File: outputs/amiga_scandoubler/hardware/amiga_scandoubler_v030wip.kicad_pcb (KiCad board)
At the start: 4 copper layers, 95 x 95 mm, 135 parts, among them J1 33DSMT1-E15SNCT, J2 33DSMT1-E15SNCT, J3 TYPE-C-31-M-12, J4 JTAG 2x05 2.54mm, U1 TVP7002PZP, U2 GW1N-LV4QN88C6/I5, U3 ADV7125KSTZ140, U4 SN74LVC2G17DBVR, U5 SN74LVC2G17DBVR, U6 SN74LVC1G17DBVR, U7 TPS62160DSGR, U8 TPS62160DSGR, U9 TPS62160DSGR, Y1 27MHz ECS-3225MVLC

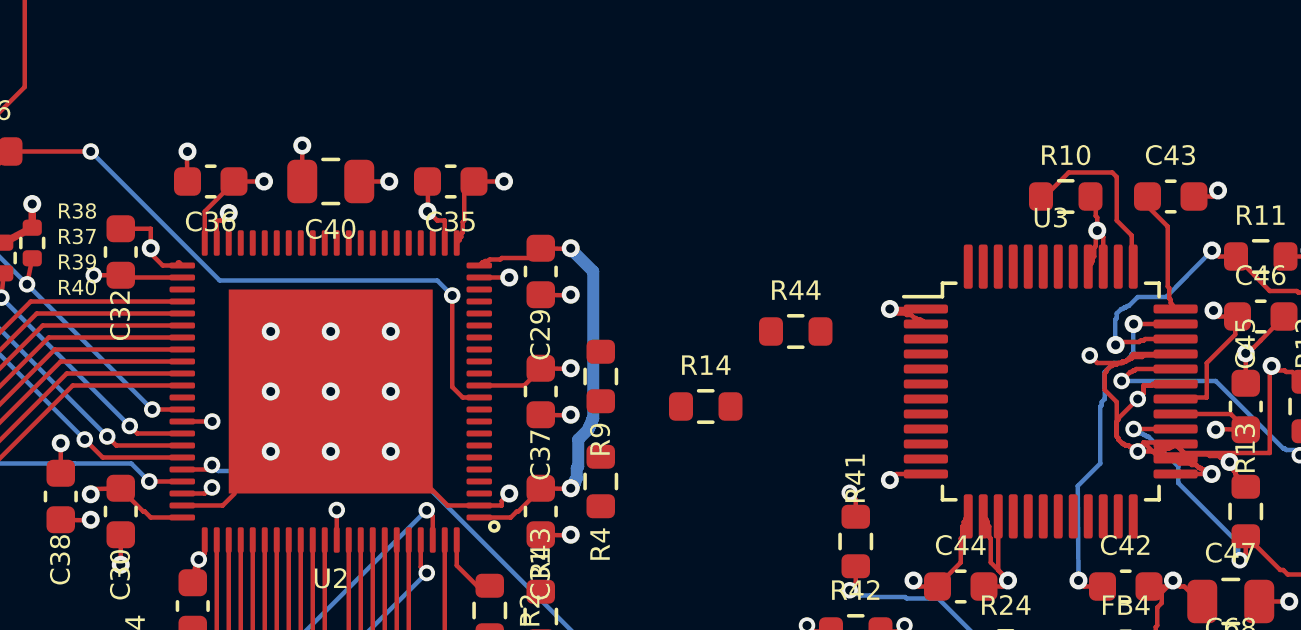
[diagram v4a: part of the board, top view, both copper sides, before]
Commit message: v030wip: 課題4 DAC_PSAVE_N(U2.56)を R44・U3.38 へ接続
- U2.56 → 内周ビア → B.Cu で EP 下 y=41 → 1V2 壁の北端を回って R44.1
- R44 → B.Cu y=39.85 → U3 本体下のビア → U3.38(パッド内側から)
- KiCad 7 DRC: エラー 0、未接続 97→95(DAC_PSAVE_N のみ)
- 導通確認、電源監査 PASS。DAC バス(課題6)への影響を記録

Co-Authored-By: Claude Opus 5.5 <noreply@anthropic.com>
Claude-Session: https://claude.ai/code/session_019f929sAJ7LRnJRRFvA6g9F
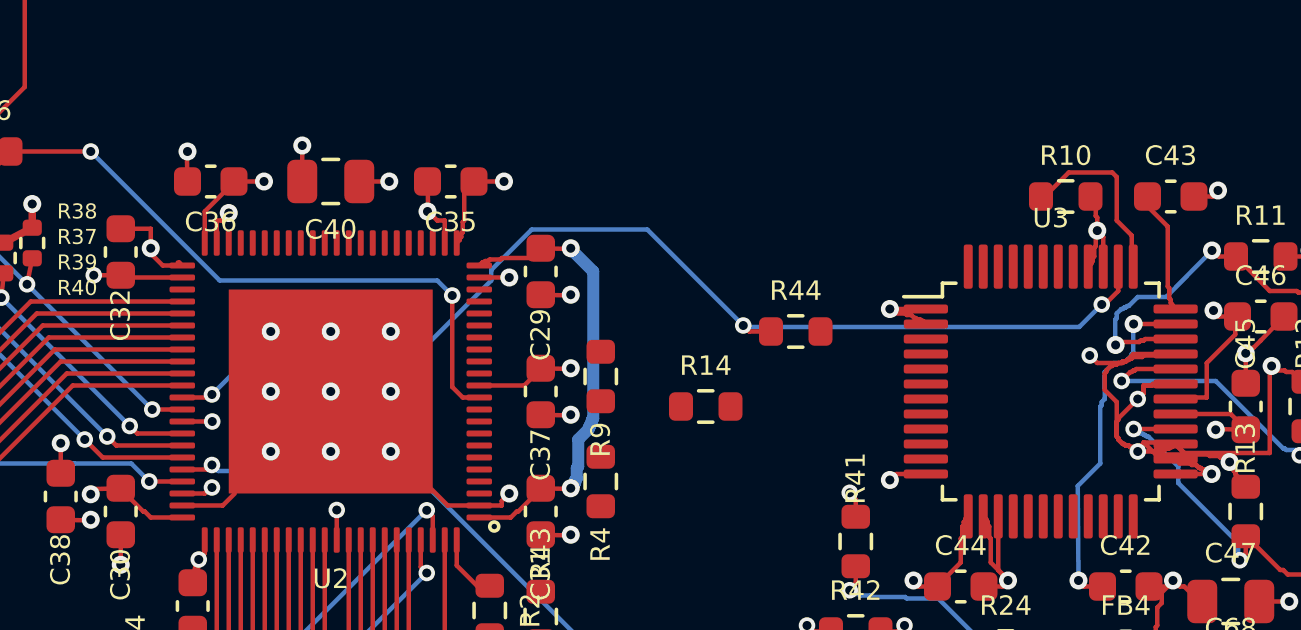
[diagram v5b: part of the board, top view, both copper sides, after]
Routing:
- net DAC_PSAVE_N: track 0.00 -> 37.4 mm, vias 0 -> 3
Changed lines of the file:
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@@
   (segment (start 54.2 47.8) (end 54.875 48.475) (width 0.15) (layer "F.Cu") (net 59))
   (segment (start 54.875 48.475) (end 55.3 48.475) (width 0.15) (layer "F.Cu") (net 59))
+  (segment (start 63.75 39.8) (end 63.95 40) (width 0.15) (layer "F.Cu") (net 60))
+  (segment (start 76.25 38.65) (end 76.25 37.837) (width 0.15) (layer "F.Cu") (net 60))
+  (segment (start 75.7 39.1) (end 75.8 39.1) (width 0.15) (layer "F.Cu") (net 60))
+  (segment (start 63.95 40) (end 64.675 40) (width 0.15) (layer "F.Cu") (net 60))
+  (segment (start 75.8 39.1) (end 76.25 38.65) (width 0.15) (layer "F.Cu") (net 60))
+  (segment (start 45.94 42.2) (end 46.04 42.1) (width 0.15) (layer "F.Cu") (net 60))
+  (segment (start 45.05 42.2) (end 45.94 42.2) (width 0.15) (layer "F.Cu") (net 60))
+  (via (at 75.7 39.1) (size 0.55) (drill 0.3) (layers "F.Cu" "B.Cu") (net 60))
+  (via (at 46.04 42.1) (size 0.55) (drill 0.3) (layers "F.Cu" "B.Cu") (net 60))
+  (via (at 63.75 39.8) (size 0.55) (drill 0.3) (layers "F.Cu" "B.Cu") (net 60))
+  (segment (start 46.04 42.1) (end 47.14 41) (width 0.15) (layer "B.Cu") (net 60))
+  (segment (start 63.8 39.85) (end 74.95 39.85) (width 0.15) (layer "B.Cu") (net 60))
+  (segment (start 56.7 36.6) (end 60.55 36.6) (width 0.15) (layer "B.Cu") (net 60))
+  (segment (start 60.55 36.6) (end 63.75 39.8) (width 0.15) (layer "B.Cu") (net 60))
+  (segment (start 63.75 39.8) (end 63.8 39.85) (width 0.15) (layer "B.Cu") (net 60))
+  (segment (start 55.35 38.3) (end 55.35 37.95) (width 0.15) (layer "B.Cu") (net 60))
+  (segment (start 55.35 37.95) (end 56.7 36.6) (width 0.15) (layer "B.Cu") (net 60))
+  (segment (start 52.65 41) (end 55.35 38.3) (width 0.15) (layer "B.Cu") (net 60))
+  (segment (start 47.14 41) (end 52.65 41) (width 0.15) (layer "B.Cu") (net 60))
+  (segment (start 74.95 39.85) (end 75.7 39.1) (width 0.15) (layer "B.Cu") (net 60))
   (segment (start 80.85 53.45) (end 80.65 53.25) (width 0.15) (layer "F.Cu") (net 62))
   (segment (start 67.5 48.4) (end 67.3 48.6) (width 0.15) (layer "F.Cu") (net 62))

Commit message: v030wip: 課題5の準備 — 1V2 右リンクを In2 へ、PSAVE を南回りへ変更
- 1V2 の右側 B.Cu 壁(58,37.225)↔(58,45.225)を同形状で In2.Cu へ移動
- DAC_PSAVE_N の U2→R44 区間を y=42.75 → 南東 → y=46 → 北東の経路に変更
  (JTAG を B.Cu で北上させる通路 x 55.4–60 を確保するため)
- KiCad 7 DRC: エラー 0、未接続 95 で変化なし。導通確認、電源監査 PASS
- 右辺の現状分析を CLAUDE.md に記録

Co-Authored-By: Claude Opus 5.5 <noreply@anthropic.com>
Claude-Session: https://claude.ai/code/session_019f929sAJ7LRnJRRFvA6g9F
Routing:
- net DAC_PSAVE_N: track 37.4 -> 38.9 mm
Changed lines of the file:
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@@
   (via (at 46.04 42.1) (size 0.55) (drill 0.3) (layers "F.Cu" "B.Cu") (net 60))
   (via (at 63.75 39.8) (size 0.55) (drill 0.3) (layers "F.Cu" "B.Cu") (net 60))
-  (segment (start 46.04 42.1) (end 47.14 41) (width 0.15) (layer "B.Cu") (net 60))
   (segment (start 63.8 39.85) (end 74.95 39.85) (width 0.15) (layer "B.Cu") (net 60))
-  (segment (start 56.7 36.6) (end 60.55 36.6) (width 0.15) (layer "B.Cu") (net 60))
-  (segment (start 60.55 36.6) (end 63.75 39.8) (width 0.15) (layer "B.Cu") (net 60))
+  (segment (start 59.45 46) (end 63.75 41.7) (width 0.15) (layer "B.Cu") (net 60))
+  (segment (start 55.7 46) (end 59.45 46) (width 0.15) (layer "B.Cu") (net 60))
+  (segment (start 46.04 42.1) (end 46.69 42.75) (width 0.15) (layer "B.Cu") (net 60))
   (segment (start 63.75 39.8) (end 63.8 39.85) (width 0.15) (layer "B.Cu") (net 60))
-  (segment (start 55.35 38.3) (end 55.35 37.95) (width 0.15) (layer "B.Cu") (net 60))
-  (segment (start 55.35 37.95) (end 56.7 36.6) (width 0.15) (layer "B.Cu") (net 60))
-  (segment (start 52.65 41) (end 55.35 38.3) (width 0.15) (layer "B.Cu") (net 60))
-  (segment (start 47.14 41) (end 52.65 41) (width 0.15) (layer "B.Cu") (net 60))
+  (segment (start 46.69 42.75) (end 52.45 42.75) (width 0.15) (layer "B.Cu") (net 60))
+  (segment (start 52.45 42.75) (end 55.7 46) (width 0.15) (layer "B.Cu") (net 60))
+  (segment (start 63.75 41.7) (end 63.75 39.8) (width 0.15) (layer "B.Cu") (net 60))
   (segment (start 74.95 39.85) (end 75.7 39.1) (width 0.15) (layer "B.Cu") (net 60))
   (segment (start 80.85 53.45) (end 80.65 53.25) (width 0.15) (layer "F.Cu") (net 62))
@@
   (segment (start 48.95 51.5) (end 46.55 49.1) (width 0.4) (layer "In2.Cu") (net 97))
   (segment (start 53.6 49.8) (end 53.6 49.85) (width 0.4) (layer "In2.Cu") (net 97))
+  (segment (start 58.25 43.6) (end 58.6 43.25) (width 0.4) (layer "In2.Cu") (net 97))
   (segment (start 42.4 45.65) (end 42.35 45.6) (width 0.4) (layer "In2.Cu") (net 97))
   (segment (start 45.9 49.1) (end 42.45 45.65) (width 0.4) (layer "In2.Cu") (net 97))
+  (segment (start 58.25 44.5) (end 58.25 43.6) (width 0.4) (layer "In2.Cu") (net 97))
   (segment (start 42.25 45.55) (end 42.1 45.55) (width 0.4) (layer "In2.Cu") (net 97))
+  (segment (start 58.7 42.95) (end 58.75 42.9) (width 0.4) (layer "In2.Cu") (net 97))
+  (segment (start 58.6 43.25) (end 58.6 43.2) (width 0.4) (layer "In2.Cu") (net 97))
   (segment (start 53.75 49.65) (end 53.6 49.8) (width 0.4) (layer "In2.Cu") (net 97))
   (segment (start 55.95 47.4) (end 53.75 49.6) (width 0.4) (layer "In2.Cu") (net 97))
   (segment (start 57.65 48.5) (end 54.85 48.5) (width 0.4) (layer "In2.Cu") (net 97))
+  (segment (start 58.7 43.05) (end 58.7 42.95) (width 0.4) (layer "In2.Cu") (net 97))
   (segment (start 70.65 66.3) (end 70.65 66.35) (width 0.4) (layer "In2.Cu") (net 97))
   (segment (start 42.35 45.6) (end 42.3 45.6) (width 0.4) (layer "In2.Cu") (net 97))
@@
   (segment (start 53.6 49.85) (end 51.95 51.5) (width 0.4) (layer "In2.Cu") (net 97))
   (segment (start 58 45.225) (end 55.95 47.3) (width 0.4) (layer "In2.Cu") (net 97))
+  (segment (start 58.65 43.15) (end 58.65 43.1) (width 0.4) (layer "In2.Cu") (net 97))
+  (segment (start 58.2 44.55) (end 58.25 44.5) (width 0.4) (layer "In2.Cu") (net 97))
   (segment (start 42.45 45.65) (end 42.4 45.65) (width 0.4) (layer "In2.Cu") (net 97))
+  (segment (start 58.1 45.15) (end 58.1 45.1) (width 0.4) (layer "In2.Cu") (net 97))
   (segment (start 51.95 51.5) (end 48.95 51.5) (width 0.4) (layer "In2.Cu") (net 97))
+  (segment (start 58.75 42.9) (end 58.75 38) (width 0.4) (layer "In2.Cu") (net 97))
+  (segment (start 58.65 43.1) (end 58.7 43.05) (width 0.4) (layer "In2.Cu") (net 97))
+  (segment (start 58.6 43.2) (end 58.65 43.15) (width 0.4) (layer "In2.Cu") (net 97))
   (segment (start 46.55 49.1) (end 45.9 49.1) (width 0.4) (layer "In2.Cu") (net 97))
   (segment (start 70.65 66.35) (end 77.05 72.75) (width 0.4) (layer "In2.Cu") (net 97))
   (segment (start 60.45 51.3) (end 57.65 48.5) (width 0.4) (layer "In2.Cu") (net 97))
+  (segment (start 58.75 38) (end 58 37.25) (width 0.4) (layer "In2.Cu") (net 97))
+  (segment (start 58.15 44.95) (end 58.2 44.9) (width 0.4) (layer "In2.Cu") (net 97))
   (segment (start 60.45 51.3) (end 60.45 56.1) (width 0.4) (layer "In2.Cu") (net 97))
   (segment (start 44 37.225) (end 58 37.225) (width 0.4) (layer "In2.Cu") (net 97))
+  (segment (start 58.2 44.9) (end 58.2 44.55) (width 0.4) (layer "In2.Cu") (net 97))
   (segment (start 60.45 56.1) (end 70.65 66.3) (width 0.4) (layer "In2.Cu") (net 97))
   (segment (start 53.75 49.6) (end 53.75 49.65) (width 0.4) (layer "In2.Cu") (net 97))
+  (segment (start 58 45.225) (end 58.1 45.15) (width 0.4) (layer "In2.Cu") (net 97))
   (segment (start 42.1 45.55) (end 42 45.45) (width 0.4) (layer "In2.Cu") (net 97))
+  (segment (start 58.15 45.05) (end 58.15 44.95) (width 0.4) (layer "In2.Cu") (net 97))
+  (segment (start 58 37.25) (end 58 37.225) (width 0.4) (layer "In2.Cu") (net 97))
+  (segment (start 58.1 45.1) (end 58.15 45.05) (width 0.4) (layer "In2.Cu") (net 97))
   (segment (start 42.3 45.6) (end 42.25 45.55) (width 0.4) (layer "In2.Cu") (net 97))
   (segment (start 42 45.45) (end 42 45.425001) (width 0.4) (layer "In2.Cu") (net 97))
-  (segment (start 58.25 43.6) (end 58.6 43.25) (width 0.4) (layer "B.Cu") (net 97))
-  (segment (start 58.25 44.5) (end 58.25 43.6) (width 0.4) (layer "B.Cu") (net 97))
-  (segment (start 58.7 42.95) (end 58.75 42.9) (width 0.4) (layer "B.Cu") (net 97))
-  (segment (start 58.6 43.25) (end 58.6 43.2) (width 0.4) (layer "B.Cu") (net 97))
-  (segment (start 58.7 43.05) (end 58.7 42.95) (width 0.4) (layer "B.Cu") (net 97))
-  (segment (start 58.65 43.15) (end 58.65 43.1) (width 0.4) (layer "B.Cu") (net 97))
-  (segment (start 58.2 44.55) (end 58.25 44.5) (width 0.4) (layer "B.Cu") (net 97))
-  (segment (start 58.1 45.15) (end 58.1 45.1) (width 0.4) (layer "B.Cu") (net 97))
-  (segment (start 58.75 42.9) (end 58.75 38) (width 0.4) (layer "B.Cu") (net 97))
-  (segment (start 58.65 43.1) (end 58.7 43.05) (width 0.4) (layer "B.Cu") (net 97))
-  (segment (start 58.6 43.2) (end 58.65 43.15) (width 0.4) (layer "B.Cu") (net 97))
-  (segment (start 58.75 38) (end 58 37.25) (width 0.4) (layer "B.Cu") (net 97))
-  (segment (start 58.15 44.95) (end 58.2 44.9) (width 0.4) (layer "B.Cu") (net 97))
-  (segment (start 58.2 44.9) (end 58.2 44.55) (width 0.4) (layer "B.Cu") (net 97))
-  (segment (start 58 45.225) (end 58.1 45.15) (width 0.4) (layer "B.Cu") (net 97))
-  (segment (start 58.15 45.05) (end 58.15 44.95) (width 0.4) (layer "B.Cu") (net 97))
-  (segment (start 58 37.25) (end 58 37.225) (width 0.4) (layer "B.Cu") (net 97))
-  (segment (start 58.1 45.1) (end 58.15 45.05) (width 0.4) (layer "B.Cu") (net 97))
   (segment (start 77.55 49.2) (end 77.7 49.05) (width 0.15) (layer "F.Cu") (net 98))
   (segment (start 77.9 48.5) (end 78.1 48.3) (width 0.15) (layer "F.Cu") (net 98))

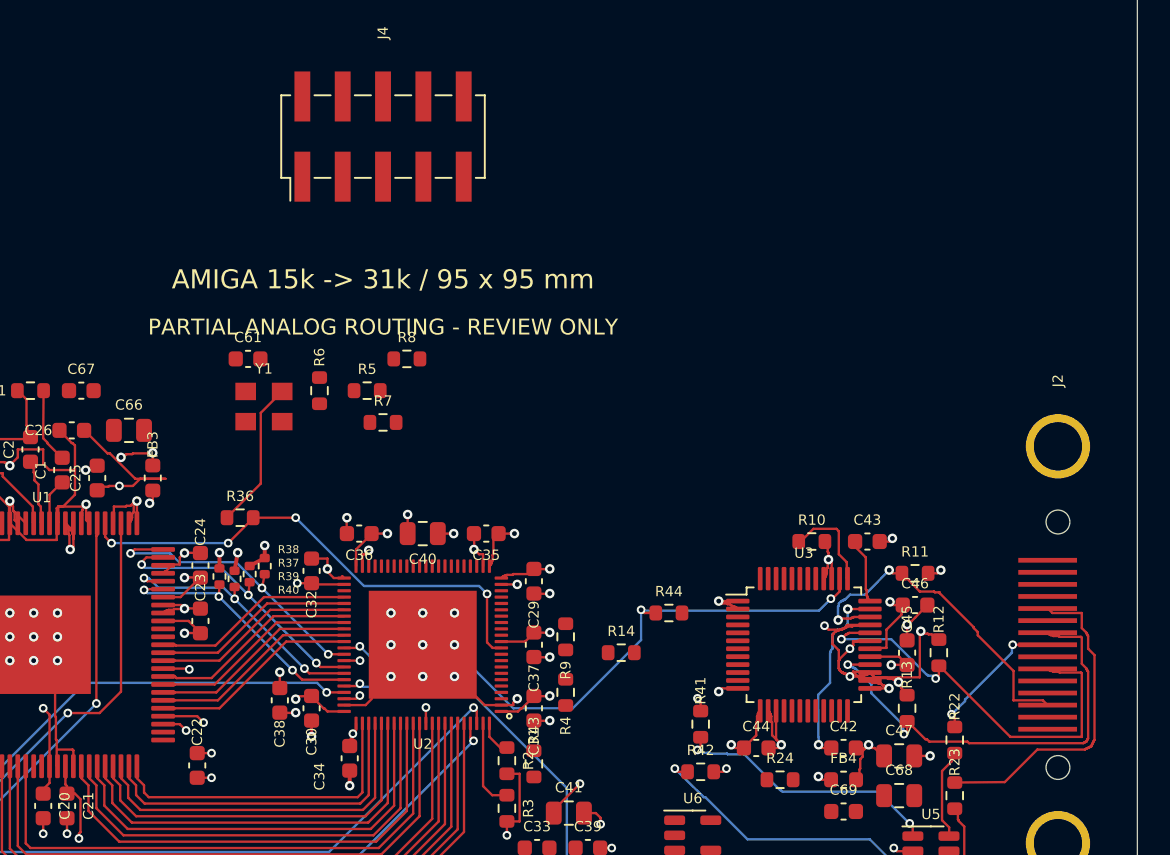
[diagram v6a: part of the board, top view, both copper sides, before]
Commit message: v030wip: 課題5 U2 右辺の JTAG 系・設定ピン(4–10番)を J4 とプルアップへ接続
- 利用者判断で C37/C31/R4/R9 を移動し、右辺正面に引き出し用の場所を確保
- pin4–9 は 0.55mm 階段状ビア、pin10 は内側ビアから B.Cu で北上
- 7 本を y=33.5 で北西へ曲げ、J4 の列位置で F.Cu に上がって J4 へ(交差なし)
- 1V2 右リンクを In2 x=55.0 へ、pin12/pin2/pin1 の電源接続を付け替え
- KiCad 7 DRC: エラー 0、未接続 95→78。導通 24 組確認、電源監査 PASS

Co-Authored-By: Claude Opus 5.5 <noreply@anthropic.com>
Claude-Session: https://claude.ai/code/session_019f929sAJ7LRnJRRFvA6g9F
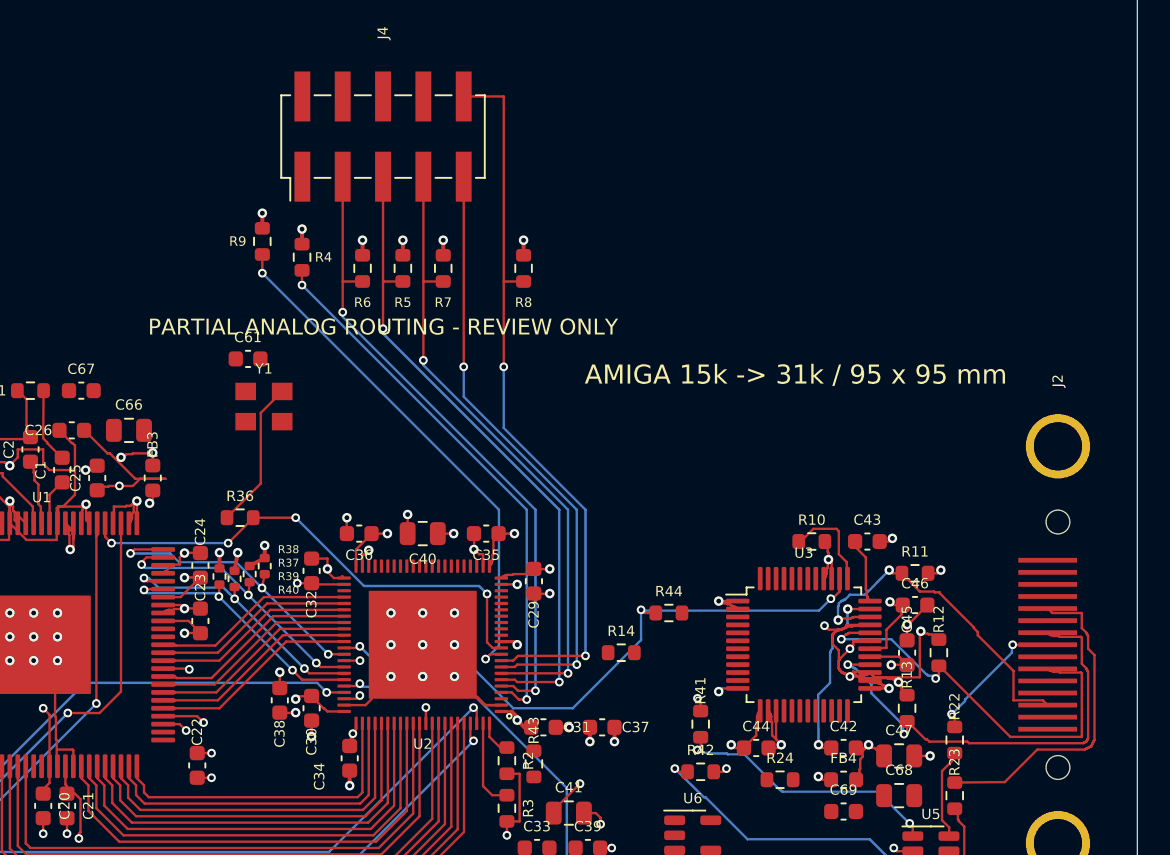
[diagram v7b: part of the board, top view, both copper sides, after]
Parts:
- moved R4 32.0 mm to (42.4, 17.6), turned to 90 degrees
- moved R9 31.4 mm to (39.9, 16.6), turned to 90 degrees
- moved R7 10.4 mm to (51.3, 18.3), turned to 90 degrees
- moved R8 9.30 mm to (56.4, 18.3), turned to 90 degrees
- moved R6 8.16 mm to (46.2, 18.3)
- moved R5 8.02 mm to (48.8, 18.3), turned to 90 degrees
- moved C37 6.75 mm to (61.3, 47.2), turned to 0 degrees
- moved C31 1.34 mm to (57.6, 47.2), turned to 0 degrees
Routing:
- net FPGA_RECONFIG_N: track 0.00 -> 46.6 mm, vias 0 -> 2
- net JTAG_TCK: track 0.00 -> 41.4 mm, vias 0 -> 2
- net JTAG_TMS: track 0.00 -> 40.9 mm, vias 0 -> 2
- net JTAG_TDI: track 0.00 -> 40.5 mm, vias 0 -> 2
- net JTAG_TDO: track 0.00 -> 38.5 mm, vias 0 -> 2
- net JTAGSEL_N: track 0.00 -> 34.7 mm, vias 0 -> 2
- net FPGA_DONE: track 0.00 -> 33.1 mm, vias 0 -> 2
- net 3V3: track 77.2 -> 79.7 mm, vias 29 -> 34
- net GND: track 346.6 -> 348.7 mm, vias 104 -> 105
- net 1V2: track 114.9 -> 113.9 mm
